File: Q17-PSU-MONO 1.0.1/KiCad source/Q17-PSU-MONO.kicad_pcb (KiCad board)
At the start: 2 copper layers, 102 x 102 mm, 38 parts, among them J1-1 AC1-1, J1-2 AC1-2, J1-3 AC2-1, J1-4 AC2-2, J2-1 V+, J2-2 V+, J2-3 GND, J2-4 GND, J2-5 GND, J2-6 V-, J2-7 V-

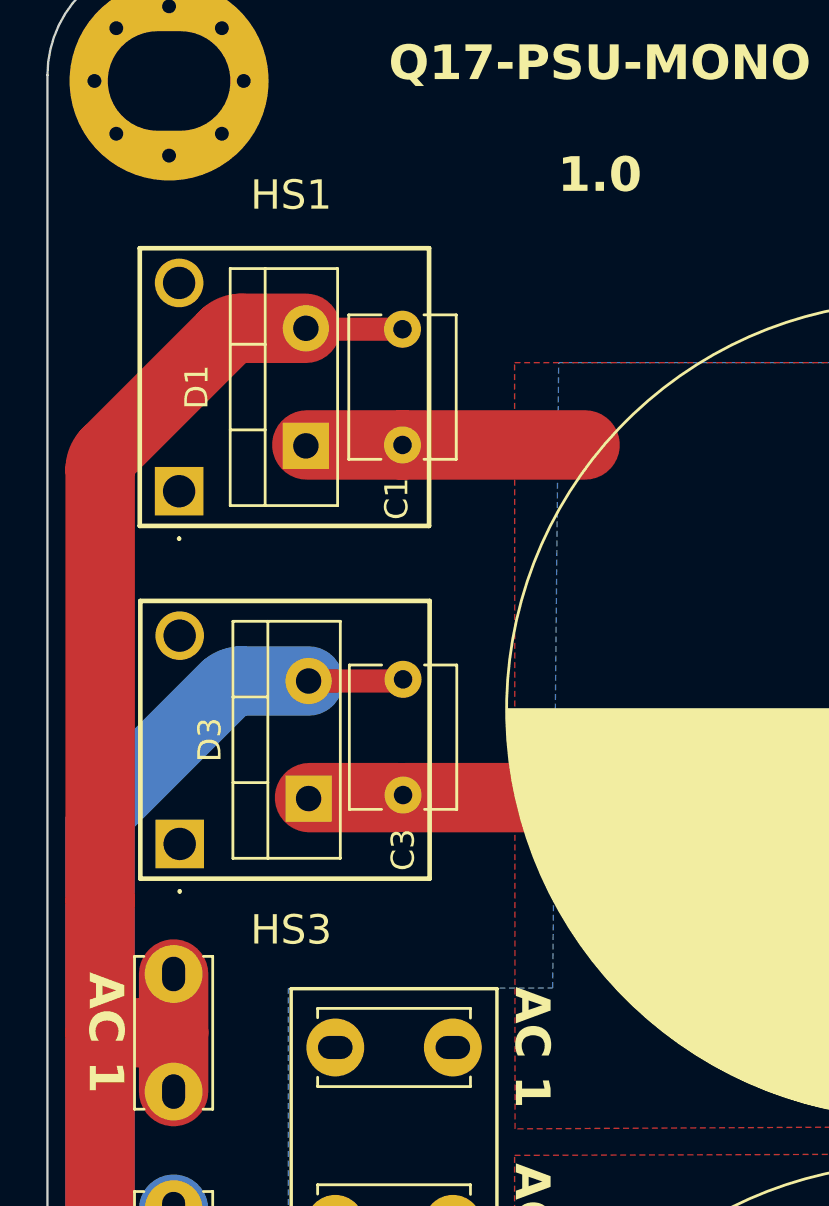
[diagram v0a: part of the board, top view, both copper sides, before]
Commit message: Updated PSU PCB.
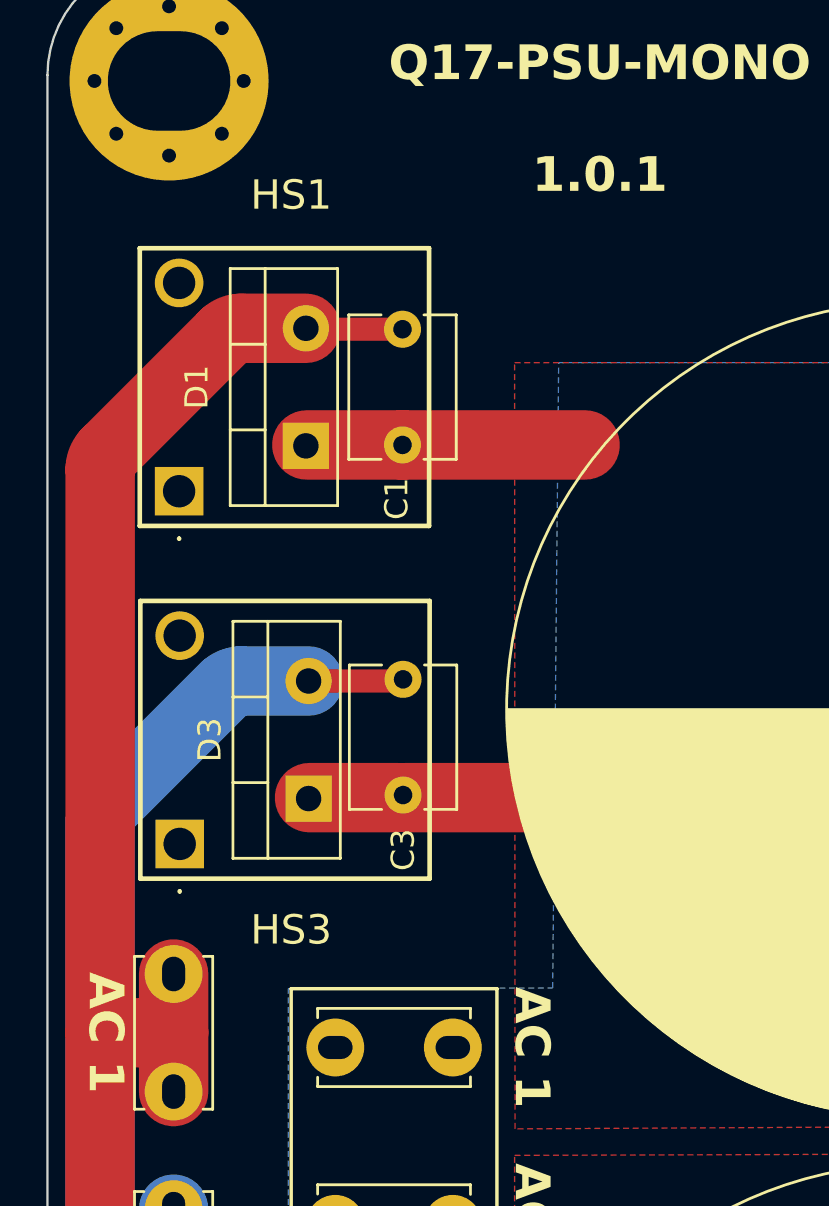
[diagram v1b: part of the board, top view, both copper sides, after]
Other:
- board text added: "Q17-PSU-MONO 1.0.1"
- board text removed: "Q17-PSU-MONO 1.0"
